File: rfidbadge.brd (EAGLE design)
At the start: 93.7 x 48.2 mm, 57 parts, among them Q1 BSS123, U1 ATMEGA328P_TQFP, U2 CLRC663, Y1 27.12 MHz

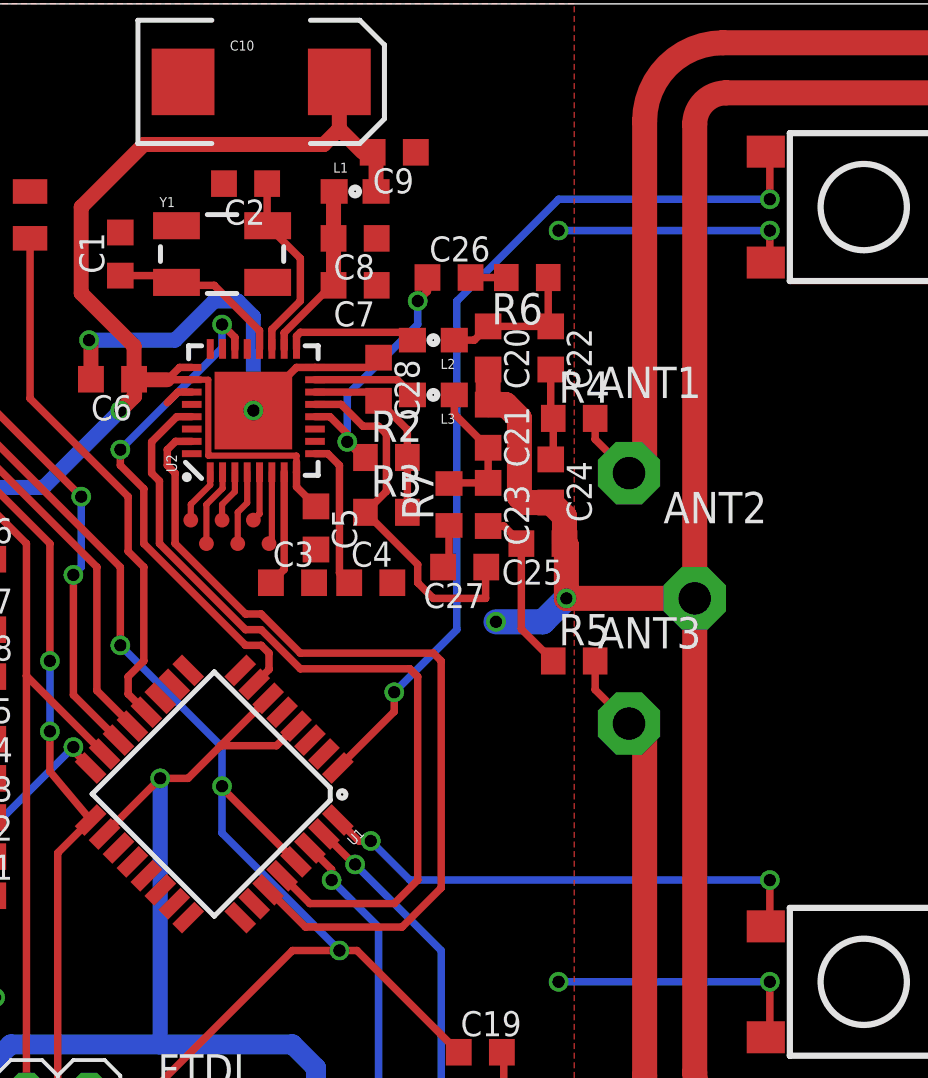
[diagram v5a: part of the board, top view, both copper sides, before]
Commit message: Connect IRQ line, move buttons
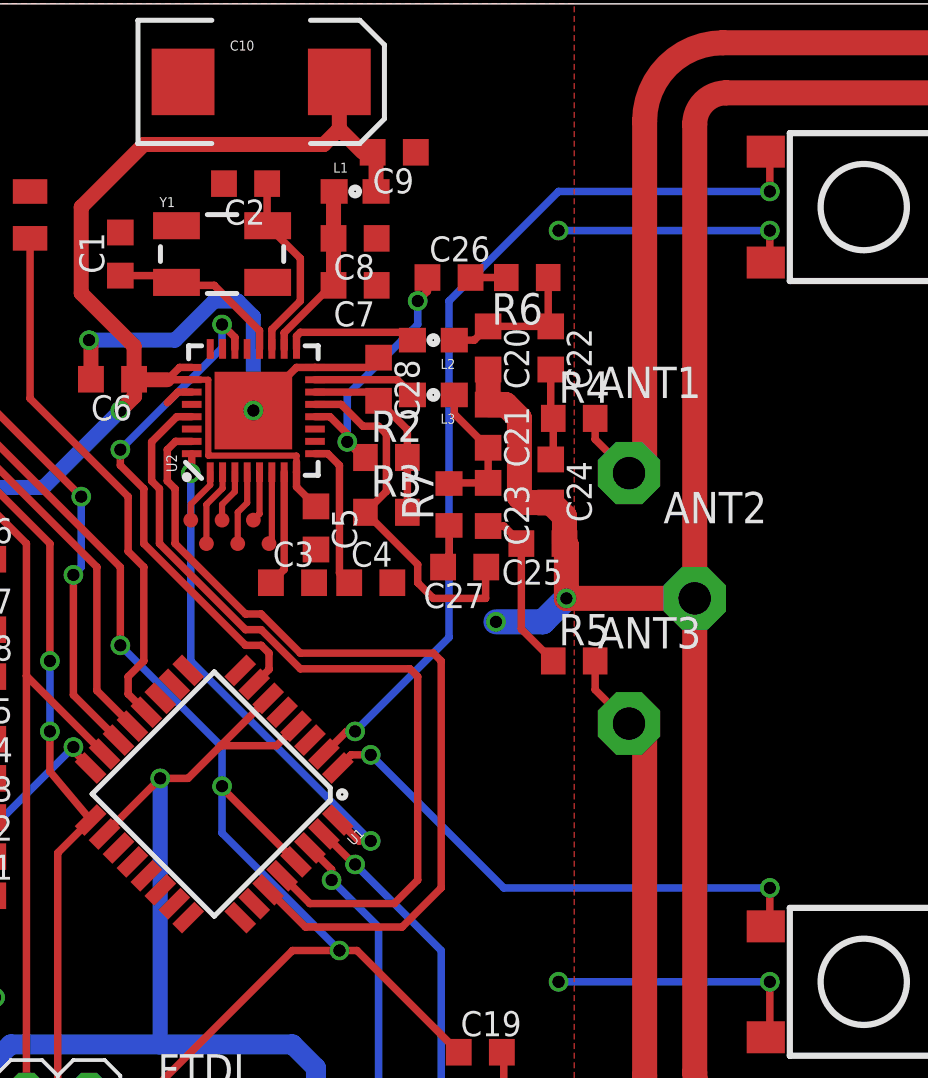
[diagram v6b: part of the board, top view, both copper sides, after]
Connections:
- new net PD4: S2.A2, U1.2
- net PD2: now also U2.32; no longer S1.A2
- net PD3: now also S1.A2; no longer S2.A2
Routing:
- net PD4: track 0.00 -> 37.3 mm, vias 0 -> 2
- net PD3: track 37.5 -> 21.7 mm
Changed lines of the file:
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@@
 <contactref element="U1" pad="27"/>
 <contactref element="U2" pad="31"/>
-<wire x1="44.49" y1="30.5" x2="43.835" y2="30.5" width="0.3048" layer="1"/>
-<wire x1="43.835" y1="30.5" x2="43.4975" y2="30.1625" width="0.3048" layer="1"/>
-<wire x1="43.4975" y1="30.1625" x2="43.4975" y2="29.5275" width="0.3048" layer="1"/>
 <wire x1="54.61" y1="21.59" x2="54.61" y2="12.3825" width="0.3048" layer="1"/>
 <wire x1="54.61" y1="12.3825" x2="53.0225" y2="10.795" width="0.3048" layer="1"/>
 <wire x1="53.0225" y1="10.795" x2="49.102940625" y2="10.795" width="0.3048" layer="1"/>
 <wire x1="49.102940625" y1="10.795" x2="47.589296875" y2="12.30864375" width="0.3048" layer="1"/>
-<wire x1="43.4975" y1="29.5275" x2="43.815" y2="29.21" width="0.3048" layer="1"/>
-<wire x1="43.815" y1="29.21" x2="43.815" y2="26.3525" width="0.3048" layer="1"/>
 <wire x1="43.815" y1="26.3525" x2="46.6725" y2="23.495" width="0.3048" layer="1"/>
 <wire x1="46.6725" y1="23.495" x2="47.3075" y2="23.495" width="0.3048" layer="1"/>
@@
 <wire x1="48.895" y1="21.9075" x2="54.2925" y2="21.9075" width="0.3048" layer="1"/>
 <wire x1="54.2925" y1="21.9075" x2="54.61" y2="21.59" width="0.3048" layer="1"/>
+<wire x1="44.49" y1="30.5" x2="43.835" y2="30.5" width="0.3048" layer="1"/>
+<wire x1="43.835" y1="30.5" x2="43.4975" y2="30.1625" width="0.3048" layer="1"/>
+<wire x1="43.4975" y1="30.1625" x2="43.4975" y2="28.8925" width="0.3048" layer="1"/>
+<wire x1="43.4975" y1="28.8925" x2="43.815" y2="28.575" width="0.3048" layer="1"/>
+<wire x1="43.815" y1="28.575" x2="43.815" y2="26.3525" width="0.3048" layer="1"/>
 </signal>
 <signal name="SCL">
 <contactref element="U1" pad="28"/>
 <contactref element="U2" pad="29"/>
-<wire x1="44.49" y1="31.5" x2="43.8825" y2="31.5" width="0.3048" layer="1"/>
-<wire x1="43.8825" y1="31.5" x2="42.8625" y2="30.48" width="0.3048" layer="1"/>
-<wire x1="42.8625" y1="30.48" x2="42.8625" y2="29.21" width="0.3048" layer="1"/>
 <wire x1="53.6575" y1="20.955" x2="53.6575" y2="12.7" width="0.3048" layer="1"/>
 <wire x1="53.6575" y1="12.7" x2="52.705" y2="11.7475" width="0.3048" layer="1"/>
 <wire x1="52.705" y1="11.7475" x2="49.281809375" y2="11.7475" width="0.3048" layer="1"/>
 <wire x1="49.281809375" y1="11.7475" x2="48.15498125" y2="12.874328125" width="0.3048" layer="1"/>
-<wire x1="42.8625" y1="29.21" x2="43.18" y2="28.8925" width="0.3048" layer="1"/>
-<wire x1="43.18" y1="28.8925" x2="43.18" y2="26.3525" width="0.3048" layer="1"/>
 <wire x1="43.18" y1="26.3525" x2="46.6725" y2="22.86" width="0.3048" layer="1"/>
 <wire x1="46.6725" y1="22.86" x2="47.3075" y2="22.86" width="0.3048" layer="1"/>
@@
 <wire x1="48.895" y1="21.2725" x2="53.34" y2="21.2725" width="0.3048" layer="1"/>
 <wire x1="53.34" y1="21.2725" x2="53.6575" y2="20.955" width="0.3048" layer="1"/>
+<wire x1="44.49" y1="31.5" x2="43.8825" y2="31.5" width="0.3048" layer="1"/>
+<wire x1="43.8825" y1="31.5" x2="42.8625" y2="30.48" width="0.3048" layer="1"/>
+<wire x1="42.8625" y1="30.48" x2="42.8625" y2="28.8925" width="0.3048" layer="1"/>
+<wire x1="42.8625" y1="28.8925" x2="43.18" y2="28.575" width="0.3048" layer="1"/>
+<wire x1="43.18" y1="28.575" x2="43.18" y2="26.3525" width="0.3048" layer="1"/>
 </signal>
 <signal name="V4">
@@
 <signal name="PD2">
 <contactref element="U1" pad="32"/>
-<contactref element="S1" pad="A2"/>
-<wire x1="67.78" y1="10.8225" x2="67.945" y2="10.8225" width="0.3048" layer="1"/>
-<wire x1="67.945" y1="10.8225" x2="67.945" y2="12.7" width="0.3048" layer="1"/>
-<via x="67.945" y="12.7" extent="1-16" drill="0.5"/>
-<wire x1="67.945" y1="12.7" x2="53.34" y2="12.7" width="0.3048" layer="16"/>
-<wire x1="53.34" y1="12.7" x2="51.7525" y2="14.2875" width="0.3048" layer="16"/>
+<contactref element="U2" pad="32"/>
+<wire x1="43.4975" y1="22.5425" x2="44.45" y2="21.59" width="0" layer="19" extent="1-16"/>
 <via x="51.7525" y="14.2875" extent="1-16" drill="0.5"/>
+<wire x1="44.45" y1="21.59" x2="51.7525" y2="14.2875" width="0.3048" layer="16"/>
 <wire x1="51.7525" y1="14.2875" x2="51.267296875" y2="14.2875" width="0.3048" layer="1"/>
 <wire x1="51.267296875" y1="14.2875" x2="50.417725" y2="15.137071875" width="0.3048" layer="1"/>
-</signal>
-<signal name="PD3">
-<contactref element="U1" pad="1"/>
-<contactref element="S2" pad="A2"/>
-<wire x1="67.78" y1="42.255" x2="67.945" y2="42.255" width="0.3048" layer="1"/>
-<wire x1="67.945" y1="42.255" x2="67.945" y2="40.3225" width="0.3048" layer="1"/>
-<via x="67.945" y="40.3225" extent="1-16" drill="0.5"/>
-<wire x1="67.945" y1="40.3225" x2="59.3725" y2="40.3225" width="0.3048" layer="16"/>
-<wire x1="59.3725" y1="40.3225" x2="55.245" y2="36.195" width="0.3048" layer="16"/>
-<wire x1="55.245" y1="36.195" x2="55.245" y2="22.86" width="0.3048" layer="16"/>
-<wire x1="55.245" y1="22.86" x2="52.705" y2="20.32" width="0.3048" layer="16"/>
-<via x="52.705" y="20.32" extent="1-16" drill="0.5"/>
-<wire x1="52.705" y1="20.32" x2="52.705" y2="19.5352" width="0.3048" layer="1"/>
-<wire x1="52.705" y1="19.5352" x2="50.417725" y2="17.247925" width="0.3048" layer="1"/>
+<wire x1="44.49" y1="30" x2="44.49" y2="29.25" width="0.3048" layer="1"/>
+<wire x1="44.49" y1="29.25" x2="44.45" y2="29.21" width="0.3048" layer="1"/>
+<via x="44.45" y="29.21" extent="1-16" drill="0.5"/>
+<wire x1="44.45" y1="29.21" x2="44.45" y2="21.59" width="0.3048" layer="16"/>
 </signal>
 <signal name="N$5">
@@
 <wire x1="47.74" y1="26.4675" x2="47.74" y2="29.25" width="0.254" layer="1"/>
 </signal>
+<signal name="PD4">
+<contactref element="U1" pad="2"/>
+<contactref element="S2" pad="A2"/>
+<wire x1="67.78" y1="42.255" x2="67.945" y2="42.255" width="0.3048" layer="1"/>
+<wire x1="67.945" y1="42.255" x2="67.945" y2="40.64" width="0.3048" layer="1"/>
+<via x="67.945" y="40.64" extent="1-16" drill="0.5"/>
+<wire x1="67.945" y1="40.64" x2="59.3725" y2="40.64" width="0.3048" layer="16"/>
+<wire x1="59.3725" y1="40.64" x2="54.9275" y2="36.195" width="0.3048" layer="16"/>
+<wire x1="54.9275" y1="36.195" x2="54.9275" y2="22.5425" width="0.3048" layer="16"/>
+<wire x1="54.9275" y1="22.5425" x2="51.1175" y2="18.7325" width="0.3048" layer="16"/>
+<via x="51.1175" y="18.7325" extent="1-16" drill="0.5"/>
+<wire x1="51.1175" y1="18.7325" x2="50.770925" y2="18.7325" width="0.3048" layer="1"/>
+<wire x1="50.770925" y1="18.7325" x2="49.8520375" y2="17.8136125" width="0.3048" layer="1"/>
+</signal>
+<signal name="PD3">
+<contactref element="U1" pad="1"/>
+<contactref element="S1" pad="A2"/>
+<wire x1="67.78" y1="10.8225" x2="67.945" y2="10.8225" width="0.3048" layer="1"/>
+<wire x1="67.945" y1="10.8225" x2="67.945" y2="12.3825" width="0.3048" layer="1"/>
+<via x="67.945" y="12.3825" extent="1-16" drill="0.5"/>
+<wire x1="67.945" y1="12.3825" x2="57.15" y2="12.3825" width="0.3048" layer="16"/>
+<wire x1="57.15" y1="12.3825" x2="51.7525" y2="17.78" width="0.3048" layer="16"/>
+<via x="51.7525" y="17.78" extent="1-16" drill="0.5"/>
+<wire x1="51.7525" y1="17.78" x2="50.9498" y2="17.78" width="0.3048" layer="1"/>
+<wire x1="50.9498" y1="17.78" x2="50.417725" y2="17.247925" width="0.3048" layer="1"/>
+</signal>
 </signals>

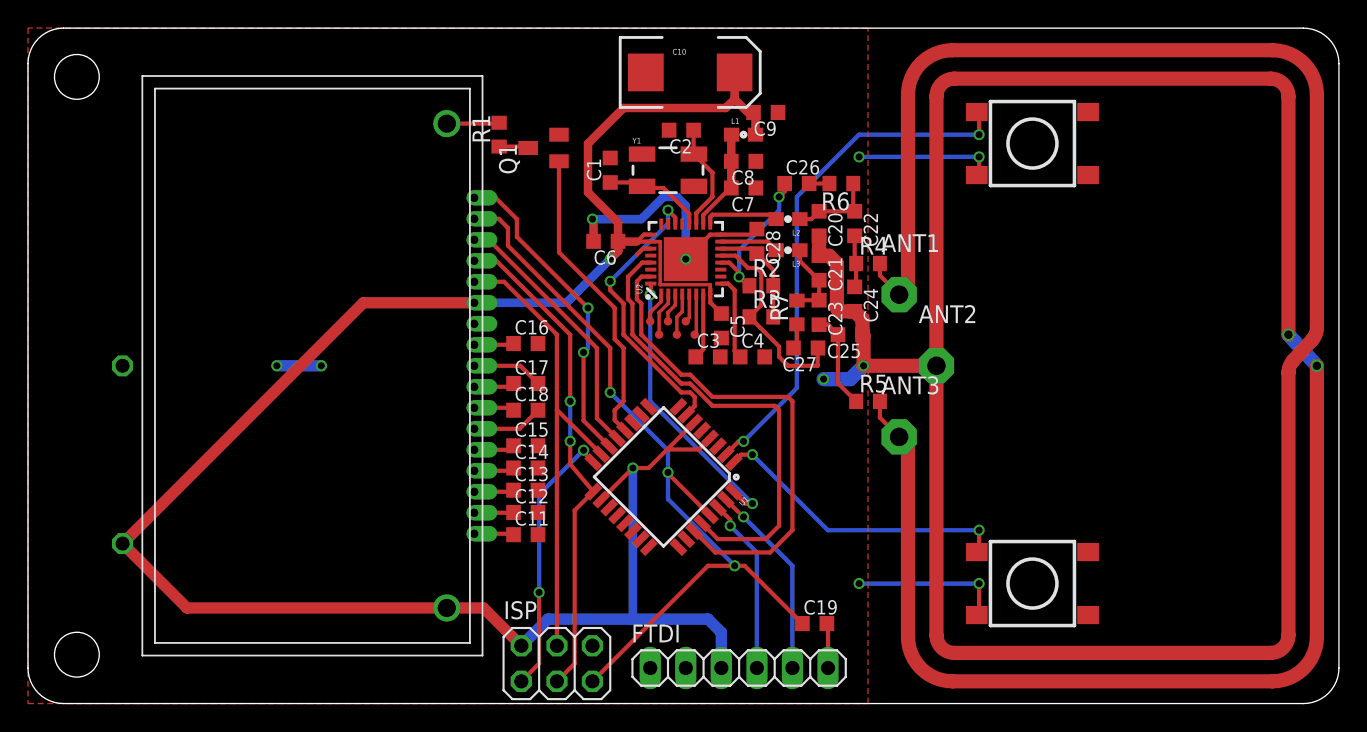
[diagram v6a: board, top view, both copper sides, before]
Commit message: Place part names
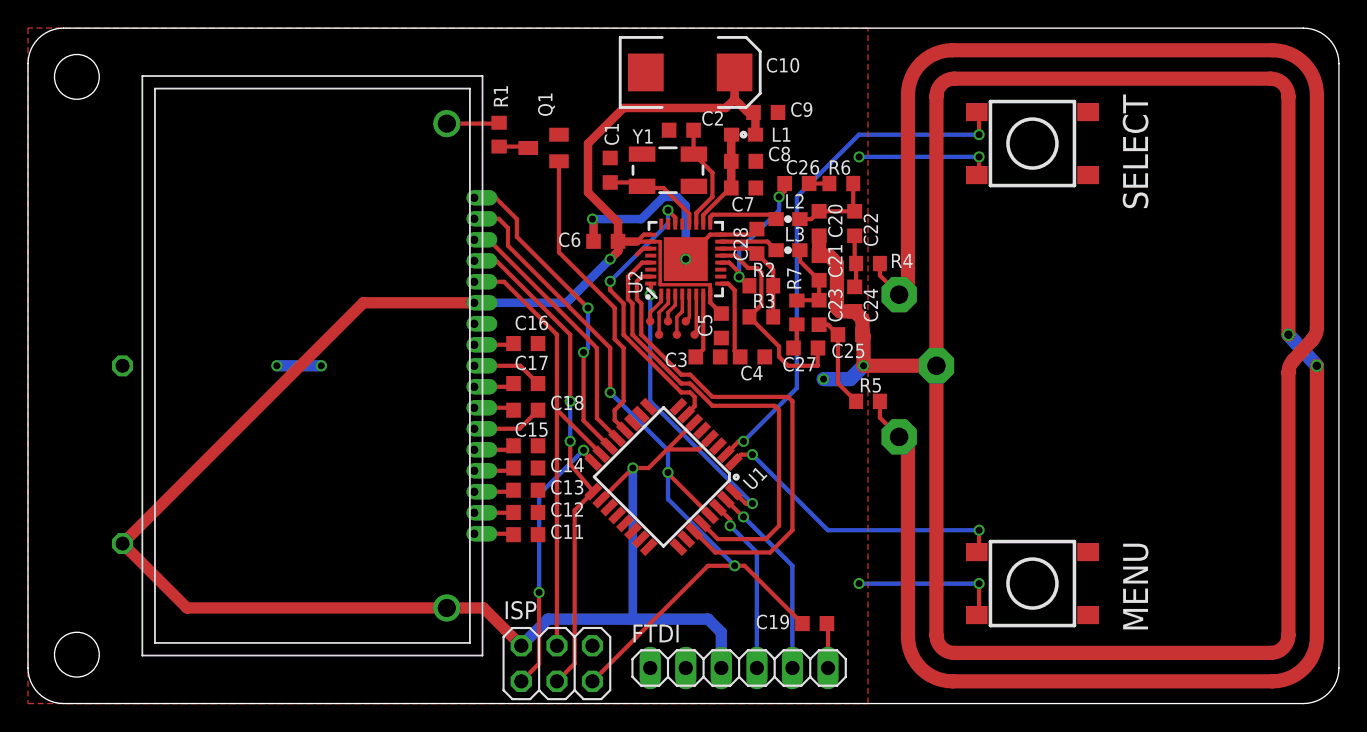
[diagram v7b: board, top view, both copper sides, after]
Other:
- board text added: "MENU"
- board text added: "SELECT"
